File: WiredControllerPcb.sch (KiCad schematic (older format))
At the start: 32 parts, among them J1 Joystick, J2 Conn_01x06, J3 Conn_01x04, J4 Conn_01x06, SW1 SW_Push, SW2 SW_Push, SW3 SW_Push, SW4 SW_Push, U1 LP2985-3.3, U2 ATmega328P-MU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

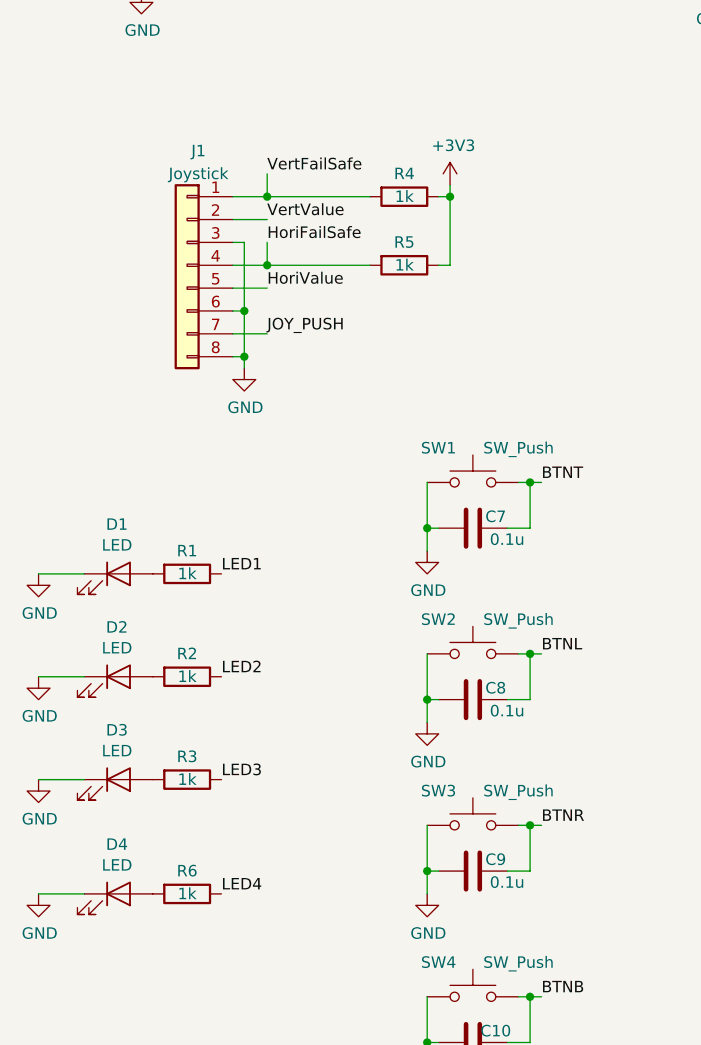
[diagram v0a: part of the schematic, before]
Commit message: Update symbol key for R4 ~ R6
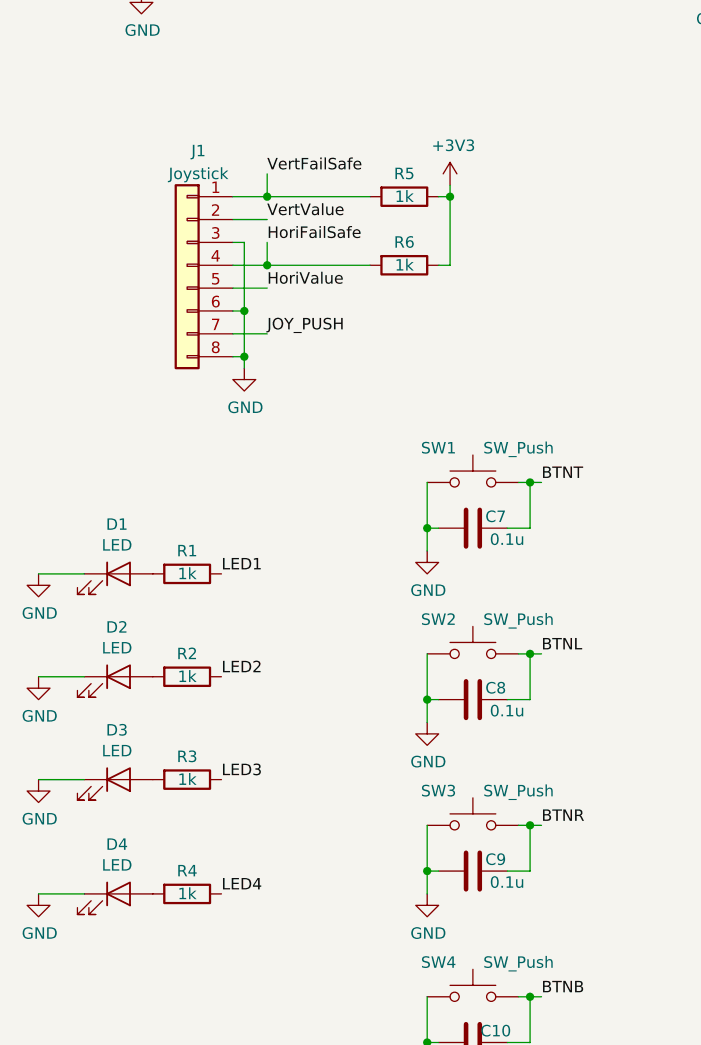
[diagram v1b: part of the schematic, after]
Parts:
- renumbered R6 to R4, R4 to R5, R5 to R6
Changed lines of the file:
@@
 $EndComp
 $Comp
-L Device:R R4
+L Device:R R5
 U 1 1 5D25E891
 P 3600 3550
-F 0 "R4" V 3500 3550 50  0000 C CNN
+F 0 "R5" V 3500 3550 50  0000 C CNN
 F 1 "1k" V 3600 3550 50  0000 C CNN
 F 2 "Resistor_SMD:R_0603_1608Metric" V 3530 3550 50  0001 C CNN
@@
 $EndComp
 $Comp
-L Device:R R5
+L Device:R R6
 U 1 1 5D2DCB51
 P 3600 3850
-F 0 "R5" V 3500 3850 50  0000 C CNN
+F 0 "R6" V 3500 3850 50  0000 C CNN
 F 1 "1k" V 3600 3850 50  0000 C CNN
 F 2 "Resistor_SMD:R_0603_1608Metric" V 3530 3850 50  0001 C CNN
@@
 	2000 6600 2200 6600
 $Comp
-L Device:R R6
+L Device:R R4
 U 1 1 5D328A3D
 P 2650 6600
-F 0 "R6" V 2550 6600 50  0000 C CNN
+F 0 "R4" V 2550 6600 50  0000 C CNN
 F 1 "1k" V 2650 6600 50  0000 C CNN
 F 2 "Resistor_SMD:R_0603_1608Metric" V 2580 6600 50  0001 C CNN

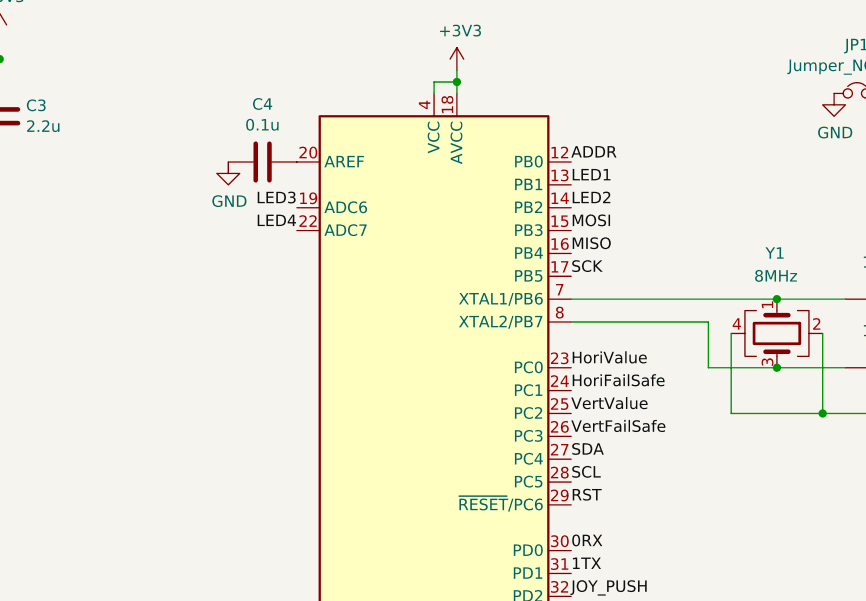
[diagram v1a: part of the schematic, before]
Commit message: Apply 2x03 pads for 6pins
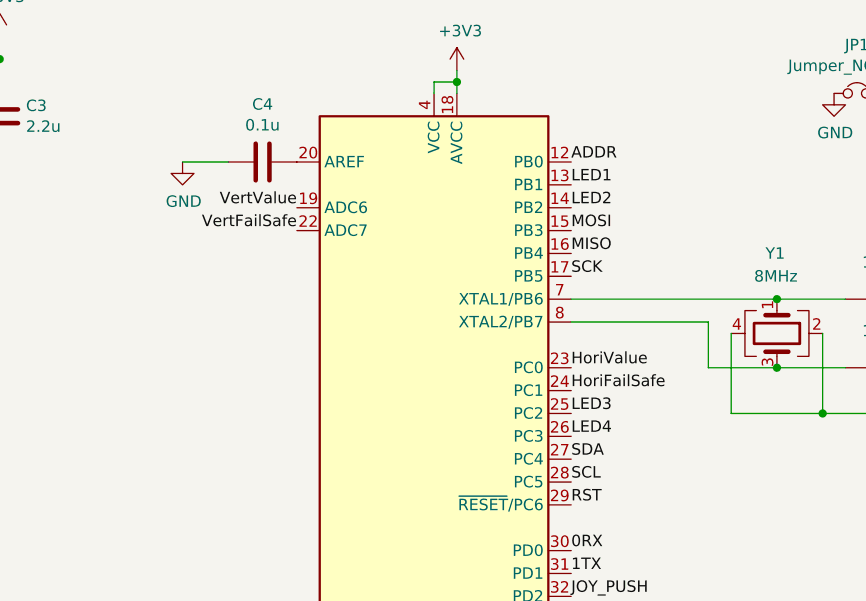
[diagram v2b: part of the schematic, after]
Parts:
- J2, J4: footprint Connector_PinHeader_2.00mm:PinHeader_2x03_P2.00mm_Vertical_SMD -> footprints:2x03_P2.54mm_Pads
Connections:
- net LED3: now also U2.25 (PC2); no longer U2.19 (ADC6)
- net LED4: now also U2.26 (PC3); no longer U2.22 (ADC7)
- net VertFailSafe: now also U2.22 (ADC7); no longer U2.26 (PC3)
- net VertValue: now also U2.19 (ADC6); no longer U2.25 (PC2)
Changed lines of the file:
@@
 L power:GND #PWR0109
 U 1 1 5D28015F
-P 4950 2600
-F 0 "#PWR0109" H 4950 2350 50  0001 C CNN
-F 1 "GND" H 4955 2427 50  0000 C CNN
-F 2 "" H 4950 2600 50  0001 C CNN
-F 3 "" H 4950 2600 50  0001 C CNN
-	1    4950 2600
+P 4750 2600
+F 0 "#PWR0109" H 4750 2350 50  0001 C CNN
+F 1 "GND" H 4755 2427 50  0000 C CNN
+F 2 "" H 4750 2600 50  0001 C CNN
+F 3 "" H 4750 2600 50  0001 C CNN
+	1    4750 2600
 	1    0    0    -1
 $EndComp
@@
 F 0 "J2" H 8868 2867 50  0000 C CNN
 F 1 "Conn_01x06" H 8868 2776 50  0000 C CNN
-F 2 "Connector_PinHeader_2.00mm:PinHeader_2x03_P2.00mm_Vertical_SMD" H 8950 2450 50  0001 C CNN
+F 2 "footprints:2x03_P2.54mm_Pads" H 8950 2450 50  0001 C CNN
 F 3 "~" H 8950 2450 50  0001 C CNN
 	1    8950 2450
@@
 Text Label 6450 3600 0    50   ~ 0
 HoriFailSafe
-Text Label 6450 3700 0    50   ~ 0
+Text Label 5250 2800 2    50   ~ 0
 VertValue
-Text Label 6450 3800 0    50   ~ 0
+Text Label 5250 2900 2    50   ~ 0
 VertFailSafe
 Wire Wire Line
@@
 Text Label 6450 2800 0    50   ~ 0
 LED2
-Text Label 5250 2800 2    50   ~ 0
+Text Label 6450 3700 0    50   ~ 0
 LED3
 Text Label 6450 4300 0    50   ~ 0
@@
 F 0 "J4" H 8868 4867 50  0000 C CNN
 F 1 "Conn_01x06" H 8868 4776 50  0000 C CNN
-F 2 "Connector_PinHeader_2.00mm:PinHeader_2x03_P2.00mm_Vertical_SMD" H 8950 4450 50  0001 C CNN
+F 2 "footprints:2x03_P2.54mm_Pads" H 8950 4450 50  0001 C CNN
 F 3 "~" H 8950 4450 50  0001 C CNN
 	1    8950 4450
@@
 Text Label 6450 2600 0    50   ~ 0
 ADDR
-Text Label 5250 2900 2    50   ~ 0
+Text Label 6450 3800 0    50   ~ 0
 LED4
 $Comp
@@
 Wire Wire Line
 	3000 4150 2850 4150
+Wire Wire Line
+	4750 2600 4950 2600
 $EndSCHEMATC

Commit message: Update crystal for bom and schema
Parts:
- Y1: footprint Crystal:Crystal_SMD_SeikoEpson_FA238-4Pin_3.2x2.5mm -> Crystal:Crystal_SMD_EuroQuartz_MJ-4Pin_5.0x3.2mm
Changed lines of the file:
@@
 F 0 "Y1" V 7000 3300 50  0000 L CNN
 F 1 "8MHz" V 7100 3250 50  0000 L CNN
-F 2 "Crystal:Crystal_SMD_SeikoEpson_FA238-4Pin_3.2x2.5mm" H 7350 3350 50  0001 C CNN
+F 2 "Crystal:Crystal_SMD_EuroQuartz_MJ-4Pin_5.0x3.2mm" H 7350 3350 50  0001 C CNN
 F 3 "~" H 7350 3350 50  0001 C CNN
 	1    7350 3350

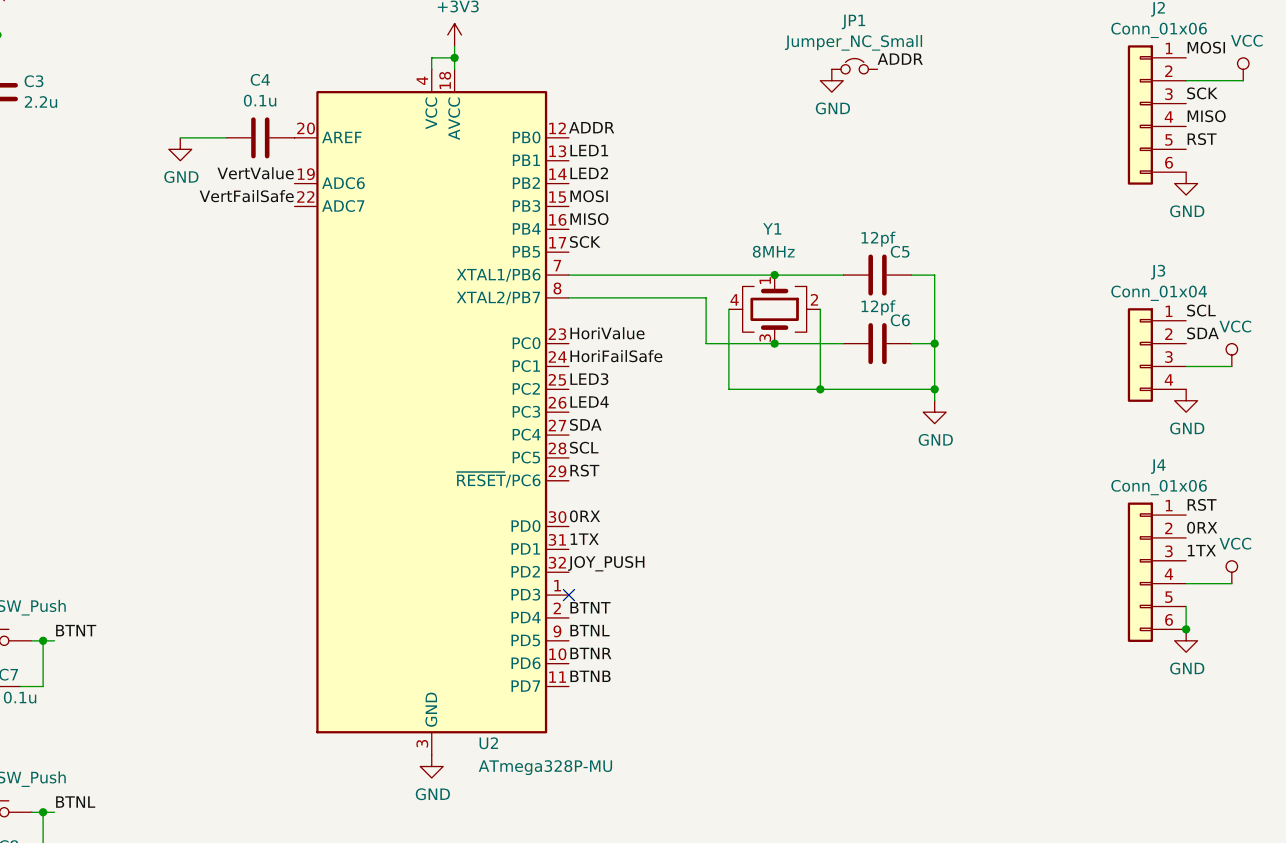
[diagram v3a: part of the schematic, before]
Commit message: Remove uart connector and use 0 and 1 to LEDs
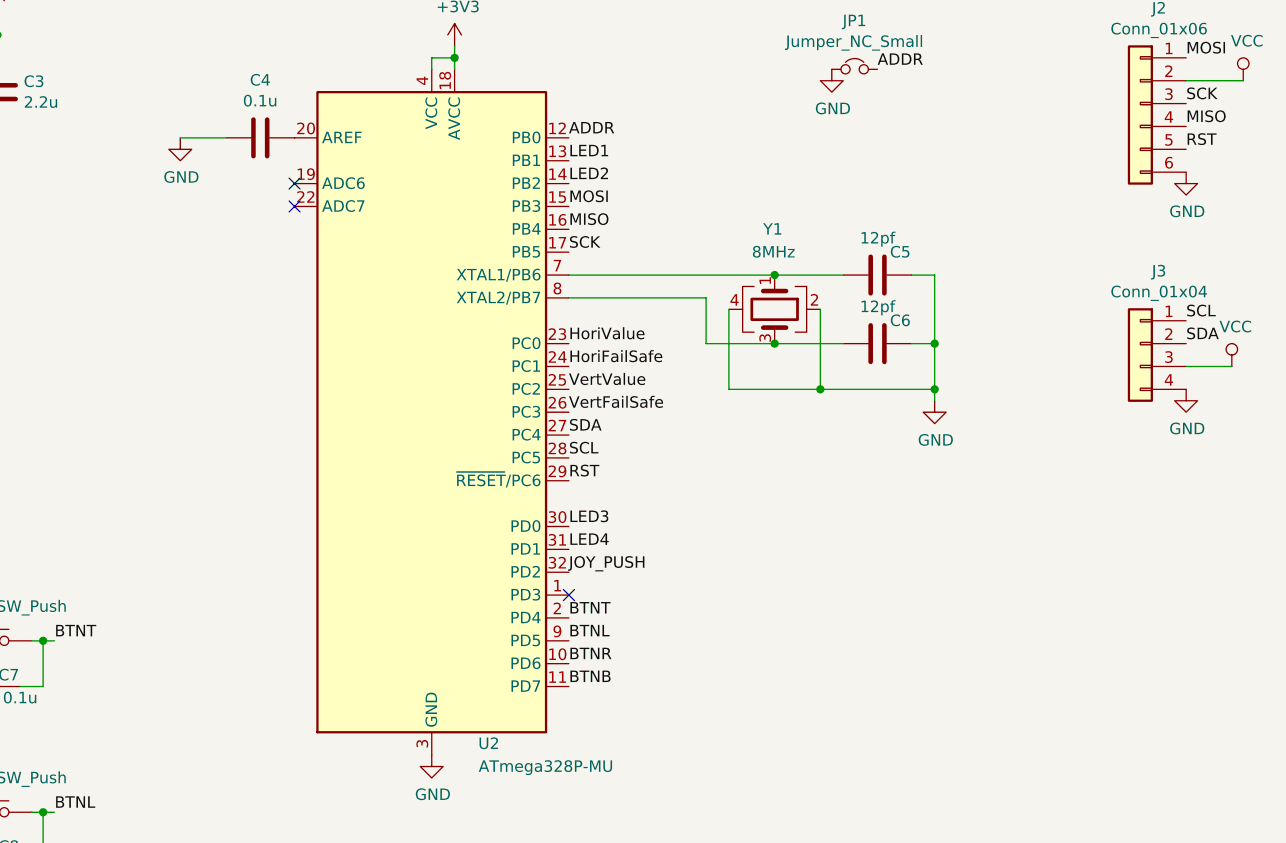
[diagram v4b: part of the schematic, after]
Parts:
- removed J4: Conn_01x06, footprints:2x03_P2.54mm_Pads, symbol Connector_Generic:Conn_01x06
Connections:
- net 0RX is gone; now on net LED3: U2.30 (PD0)
- net 1TX is gone; now on net LED4: U2.31 (PD1)
- net LED3: no longer U2.25 (PC2)
- net LED4: no longer U2.26 (PC3)
- net VertFailSafe: now also U2.26 (PC3); no longer U2.22 (ADC7)
- net VertValue: now also U2.25 (PC2); no longer U2.19 (ADC6)
- no-connect marks 1 -> 3
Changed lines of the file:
@@
 Text Label 6450 3600 0    50   ~ 0
 HoriFailSafe
-Text Label 5250 2800 2    50   ~ 0
+Text Label 6450 3700 0    50   ~ 0
 VertValue
-Text Label 5250 2900 2    50   ~ 0
+Text Label 6450 3800 0    50   ~ 0
 VertFailSafe
 Wire Wire Line
@@
 Text Label 6450 2800 0    50   ~ 0
 LED2
-Text Label 6450 3700 0    50   ~ 0
+Text Label 6450 4300 0    50   ~ 0
 LED3
-Text Label 6450 4300 0    50   ~ 0
-0RX
-Text Label 6450 4400 0    50   ~ 0
-1TX
 NoConn ~ 6450 4600
 Wire Wire Line
@@
 Text Label 6450 5000 0    50   ~ 0
 BTNB
-$Comp
-L Connector_Generic:Conn_01x06 J4
-U 1 1 5D30736F
-P 8950 4450
-F 0 "J4" H 8868 4867 50  0000 C CNN
-F 1 "Conn_01x06" H 8868 4776 50  0000 C CNN
-F 2 "footprints:2x03_P2.54mm_Pads" H 8950 4450 50  0001 C CNN
-F 3 "~" H 8950 4450 50  0001 C CNN
-	1    8950 4450
-	-1   0    0    -1
-$EndComp
-$Comp
-L power:VCC #PWR0121
-U 1 1 5D3078A4
-P 9350 4550
-F 0 "#PWR0121" H 9350 4400 50  0001 C CNN
-F 1 "VCC" H 9367 4723 50  0000 C CNN
-F 2 "" H 9350 4550 50  0001 C CNN
-F 3 "" H 9350 4550 50  0001 C CNN
-	1    9350 4550
-	1    0    0    -1
-$EndComp
-$Comp
-L power:GND #PWR0122
-U 1 1 5D309169
-P 9150 4750
-F 0 "#PWR0122" H 9150 4500 50  0001 C CNN
-F 1 "GND" H 9155 4577 50  0000 C CNN
-F 2 "" H 9150 4750 50  0001 C CNN
-F 3 "" H 9150 4750 50  0001 C CNN
-	1    9150 4750
-	1    0    0    -1
-$EndComp
-Text Label 9150 4250 0    50   ~ 0
-RST
-Text Label 9150 4450 0    50   ~ 0
-1TX
-Text Label 9150 4350 0    50   ~ 0
-0RX
-Wire Wire Line
-	9150 4650 9150 4750
-Connection ~ 9150 4750
-Wire Wire Line
-	9150 4550 9350 4550
 Text Label 6450 2600 0    50   ~ 0
 ADDR
-Text Label 6450 3800 0    50   ~ 0
+Text Label 6450 4400 0    50   ~ 0
 LED4
 $Comp
@@
 Wire Wire Line
 	4750 2600 4950 2600
+NoConn ~ 5250 2800
+NoConn ~ 5250 2900
 $EndSCHEMATC

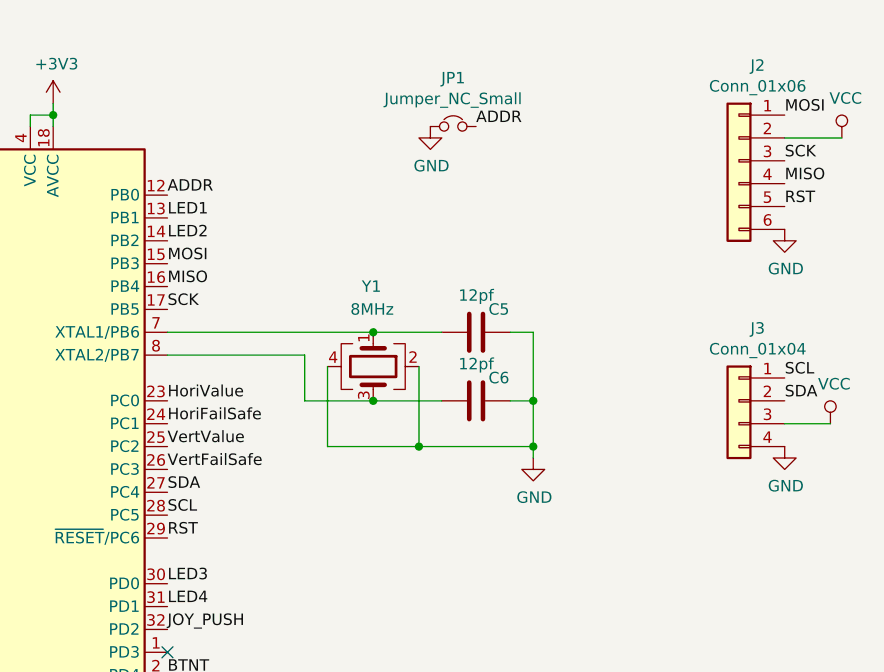
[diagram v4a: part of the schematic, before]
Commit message: Remove crystal, change leds and replace miso and mosi
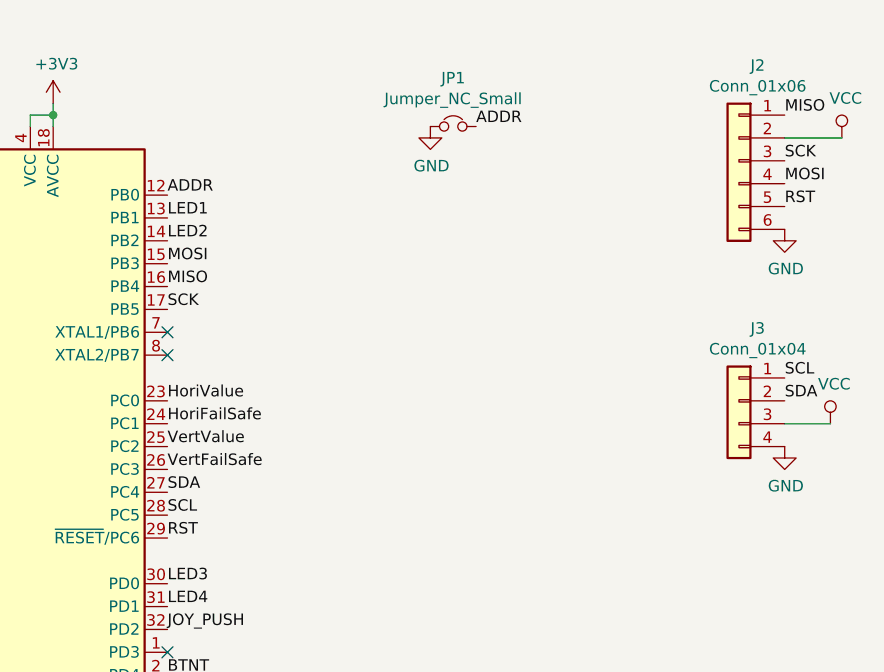
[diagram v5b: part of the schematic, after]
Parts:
- removed C5, C6: 12pf, Capacitor_SMD:C_0402_1005Metric, symbol Device:C
- removed Y1: 8MHz, Crystal:Crystal_SMD_EuroQuartz_MJ-4Pin_5.0x3.2mm, symbol Device:Crystal_GND24
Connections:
- net MISO: now also J2.1 (Pin_1); no longer J2.4 (Pin_4)
- net MOSI: now also J2.4 (Pin_4); no longer J2.1 (Pin_1)
- no-connect marks 3 -> 5
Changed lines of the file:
@@
 LED3
-$Comp
-L Device:C C5
-U 1 1 5D26CD6D
-P 7800 3200
-F 0 "C5" V 7700 3300 50  0000 C CNN
-F 1 "12pf" V 7639 3200 50  0000 C CNN
-F 2 "Capacitor_SMD:C_0402_1005Metric" H 7838 3050 50  0001 C CNN
-F 3 "~" H 7800 3200 50  0001 C CNN
-	1    7800 3200
-	0    1    1    0
-$EndComp
-$Comp
-L Device:C C6
-U 1 1 5D26D0F2
-P 7800 3500
-F 0 "C6" V 7700 3600 50  0000 C CNN
-F 1 "12pf" V 7639 3500 50  0000 C CNN
-F 2 "Capacitor_SMD:C_0402_1005Metric" H 7838 3350 50  0001 C CNN
-F 3 "~" H 7800 3500 50  0001 C CNN
-	1    7800 3500
-	0    1    1    0
-$EndComp
-$Comp
-L power:GND #PWR0106
-U 1 1 5D26F1A4
-P 8050 3750
-F 0 "#PWR0106" H 8050 3500 50  0001 C CNN
-F 1 "GND" H 8055 3577 50  0000 C CNN
-F 2 "" H 8050 3750 50  0001 C CNN
-F 3 "" H 8050 3750 50  0001 C CNN
-	1    8050 3750
-	1    0    0    -1
-$EndComp
-Wire Wire Line
-	8050 3200 7950 3200
-Wire Wire Line
-	7950 3500 8050 3500
-Connection ~ 8050 3500
-Wire Wire Line
-	8050 3500 8050 3200
 $Comp
 L power:GND #PWR0107
@@
 $EndComp
 $Comp
-L Device:Crystal_GND24 Y1
-U 1 1 5D275DE9
-P 7350 3350
-F 0 "Y1" V 7000 3300 50  0000 L CNN
-F 1 "8MHz" V 7100 3250 50  0000 L CNN
-F 2 "Crystal:Crystal_SMD_EuroQuartz_MJ-4Pin_5.0x3.2mm" H 7350 3350 50  0001 C CNN
-F 3 "~" H 7350 3350 50  0001 C CNN
-	1    7350 3350
-	0    1    1    0
-$EndComp
-Connection ~ 7350 3200
-Connection ~ 7350 3500
-Wire Wire Line
-	7050 3500 7350 3500
-Wire Wire Line
-	8050 3500 8050 3700
-Wire Wire Line
-	7350 3200 7650 3200
-Wire Wire Line
-	7350 3500 7650 3500
-Wire Wire Line
-	7150 3700 7550 3700
-Connection ~ 8050 3700
-Wire Wire Line
-	8050 3700 8050 3750
-Wire Wire Line
-	7550 3350 7550 3700
-Connection ~ 7550 3700
-Wire Wire Line
-	7550 3700 8050 3700
-$Comp
 L power:GND #PWR0109
 U 1 1 5D28015F
@@
 	-1   0    0    -1
 $EndComp
-Text Label 9150 2250 0    50   ~ 0
+Text Label 9150 2550 0    50   ~ 0
 MOSI
 Text Label 9150 2450 0    50   ~ 0
 SCK
-Text Label 9150 2550 0    50   ~ 0
+Text Label 9150 2250 0    50   ~ 0
 MISO
 Text Label 9150 2650 0    50   ~ 0
@@
 Text Label 6450 3800 0    50   ~ 0
 VertFailSafe
-Wire Wire Line
-	6450 3200 7350 3200
-Wire Wire Line
-	7050 3300 7050 3500
-Wire Wire Line
-	6450 3300 7050 3300
-Wire Wire Line
-	7150 3350 7150 3700
-Text Label 6450 2700 0    50   ~ 0
-LED1
-Text Label 6450 2800 0    50   ~ 0
-LED2
-Text Label 6450 4300 0    50   ~ 0
-LED3
 NoConn ~ 6450 4600
 Wire Wire Line
@@
 Text Label 6450 2600 0    50   ~ 0
 ADDR
-Text Label 6450 4400 0    50   ~ 0
-LED4
 $Comp
 L Device:LED D4
@@
 	4750 2600 4950 2600
 NoConn ~ 5250 2800
+Text Label 6450 4400 0    50   ~ 0
+LED4
+Text Label 6450 4300 0    50   ~ 0
+LED3
+Text Label 6450 2800 0    50   ~ 0
+LED2
+Text Label 6450 2700 0    50   ~ 0
+LED1
 NoConn ~ 5250 2900
+NoConn ~ 6450 3200
+NoConn ~ 6450 3300
 $EndSCHEMATC
